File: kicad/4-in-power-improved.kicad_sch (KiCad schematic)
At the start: 45 parts, among them J1 USB_C_Receptacle_USB2.0_16P, J2 Bus_PCI_Express_x1, J3 Conn_01x02, U1 XC6206P332MR, U2 2P SMD 2.54P Jumper, U3 W25Q128JVP, U4 2P SMD 2.54P Jumper, U5 MCP25625T-E/ML, U6 RP2040, X1 ABM8-272-T3, Y1 X322516MLB4SI

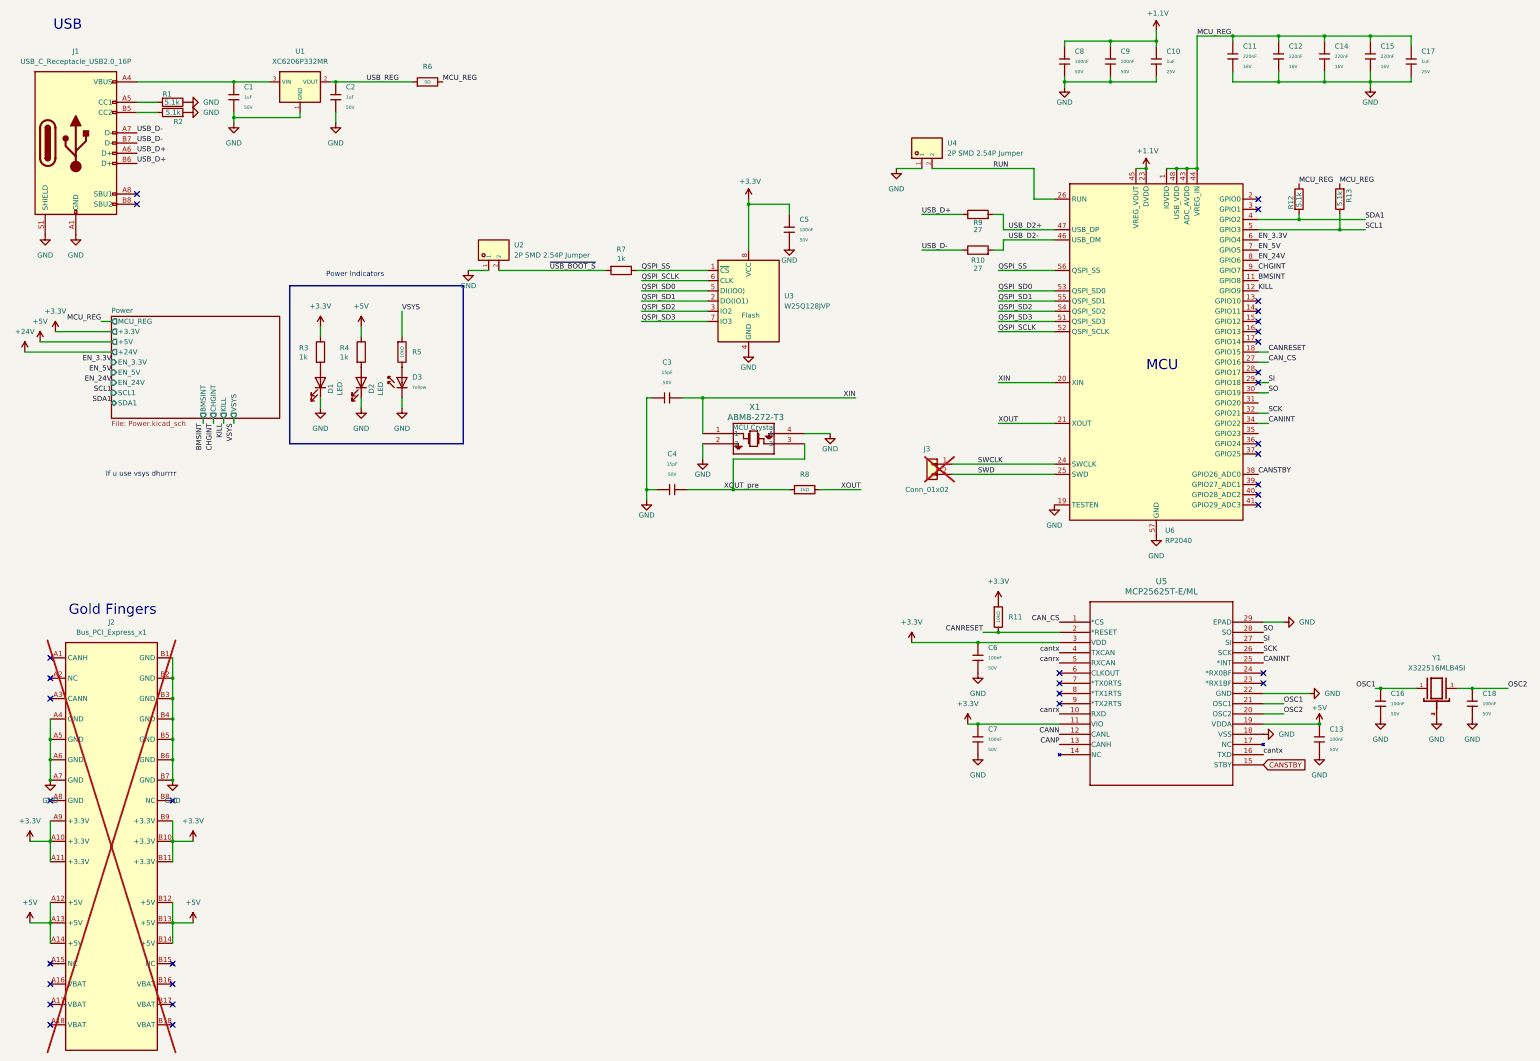
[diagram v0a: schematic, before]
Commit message: Charger IC footprint routed RP2040 routed BMS routed xt30s and balancers router
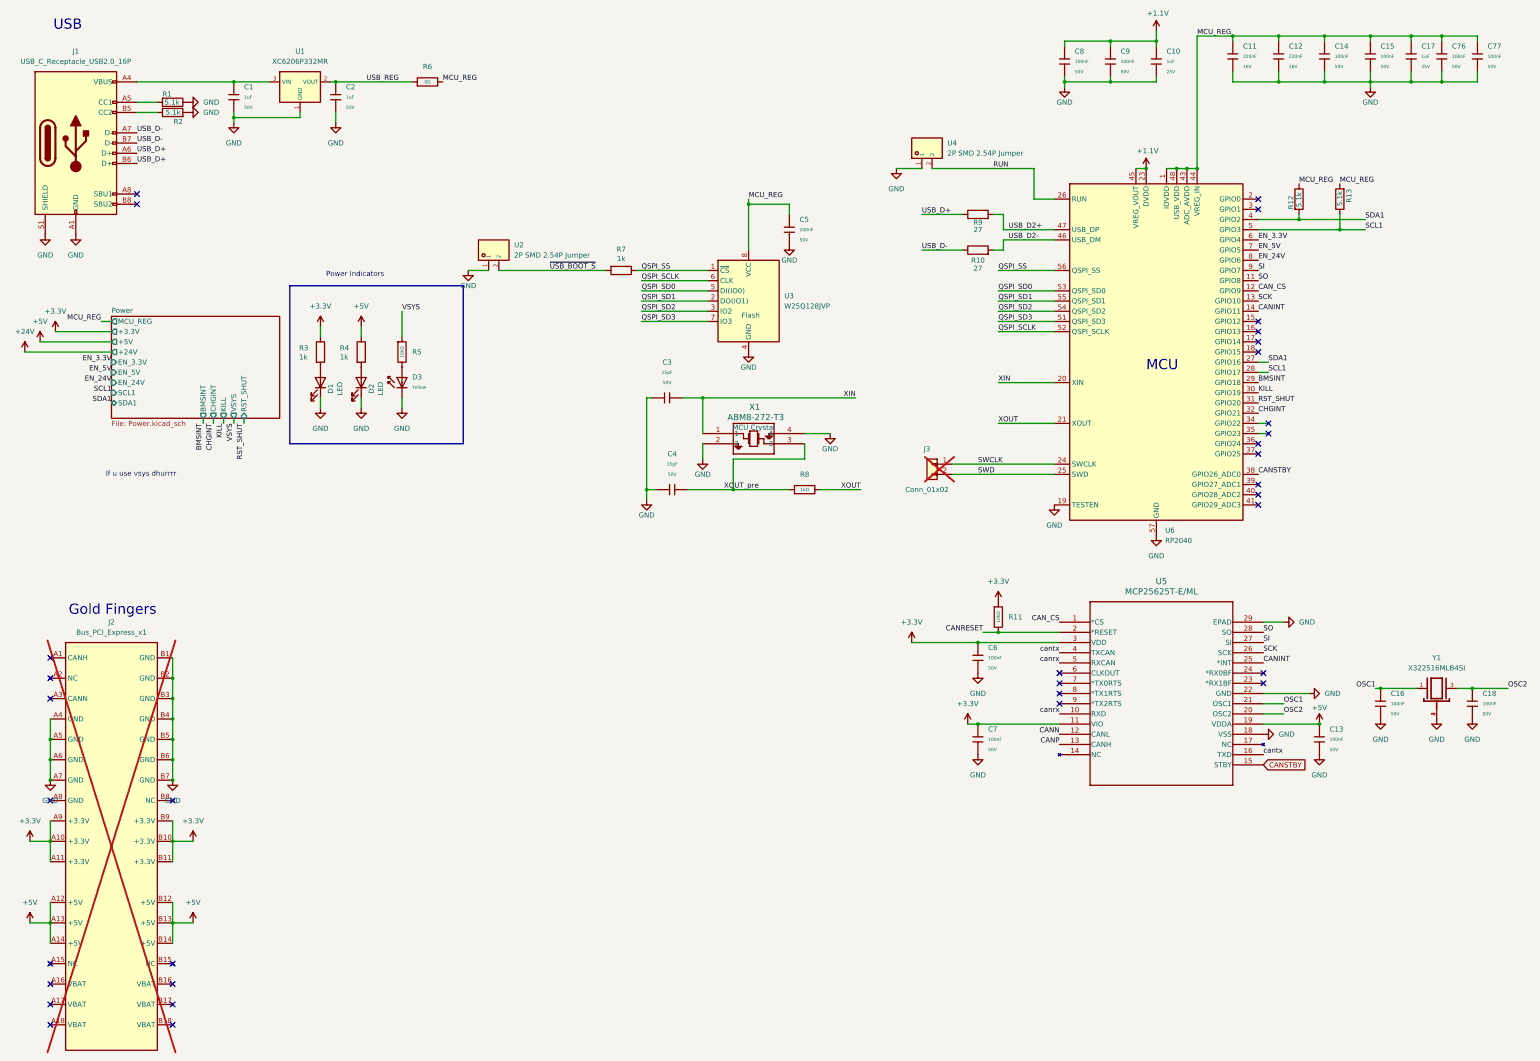
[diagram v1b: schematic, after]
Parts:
- removed C15: 220nF, PCM_JLCPCB:C_0402, symbol PCM_JLCPCB-Capacitors:0402,220nF
- removed R6: 0Ω, PCM_JLCPCB:R_0402, symbol PCM_JLCPCB-Resistors:0402,0Ω
- added C15, C76, C77: 100nF, PCM_JLCPCB:C_0402, symbol 4in-power:0402,100nF,(2)
- added R6: 0Ω, PCM_JLCPCB:R_0603, symbol PCM_JLCPCB-Resistors:0603,0Ω
- C14: value 220nF -> 100nF; symbol PCM_JLCPCB-Capacitors:0402,220nF -> 4in-power:0402,100nF,(2); Capacitance 220nF -> 100nF; LCSC C16772 -> C307331; Part CL05B224KO5NNNC -> CL05B104KB54PNC; Price 0.007USD -> 0.008USD; Stock 202070 -> 8389599; Voltage Rated 16V -> 50V
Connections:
- net +3.3V: no longer C5.1, U3.8 (VCC)
- net BMSINT: now also U6.29 (GPIO18); no longer U6.11 (GPIO8)
- net CANINT: now also U6.14 (GPIO11); no longer U6.34 (GPIO22)
- net CANRESET: no longer U6.18 (GPIO15)
- net CAN_CS: now also U6.12 (GPIO9); no longer U6.27 (GPIO16)
- net CHGINT: now also U6.32 (GPIO21); no longer U6.9 (GPIO7)
- net GND: now also C15.2, C76.2, C77.2
- net KILL: now also U6.30 (GPIO19); no longer U6.12 (GPIO9)
- net MCU_REG: now also C5.1, U3.8 (VCC), C15.1, C76.1, C77.1, R6.2
- net SCK: now also U6.13 (GPIO10); no longer U6.32 (GPIO21)
- net SCL1: now also U6.28 (GPIO17)
- net SDA1: now also U6.27 (GPIO16)
- net SI: now also U6.9 (GPIO7); no longer U6.29 (GPIO18)
- net SO: now also U6.11 (GPIO8); no longer U6.30 (GPIO19)
- net USB_REG: now also R6.1
- net RST_SHUT: now reaches U6.31 (GPIO20)
- no-connect marks 35 -> 34
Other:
- sheet Power ports: added RST_SHUT; removed none
- moved on the sheet: C17

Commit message: Footprint routing completed
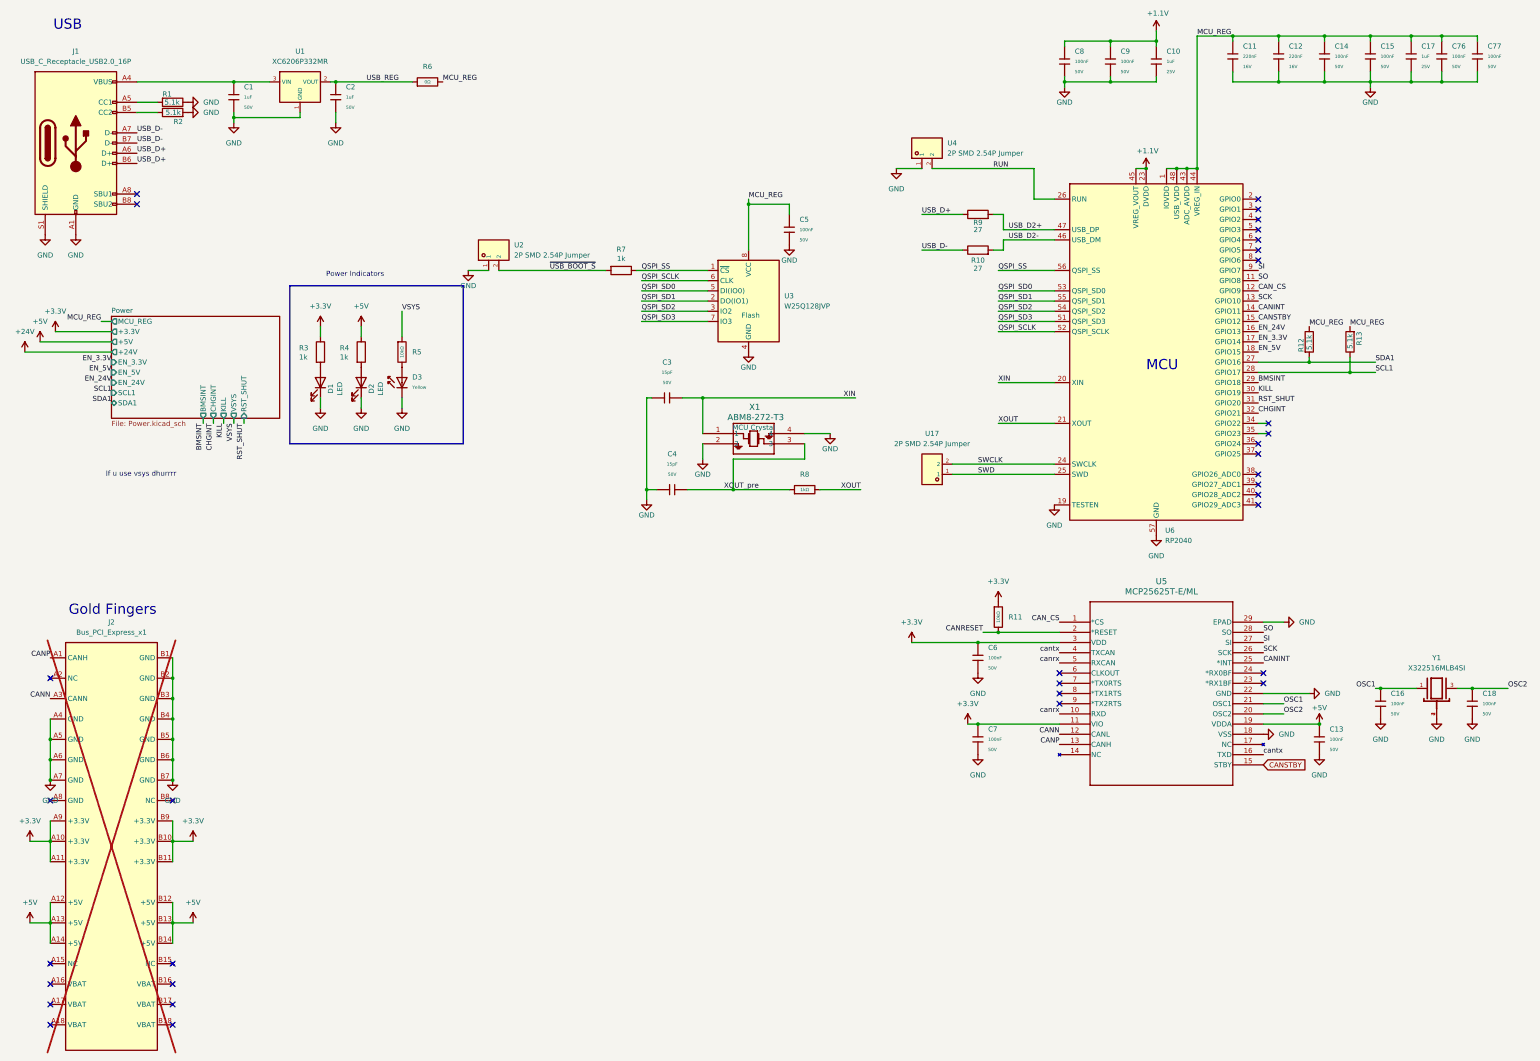
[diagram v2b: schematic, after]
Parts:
- removed J3: Conn_01x02, Connector_PinHeader_2.54mm:PinHeader_1x02_P2.54mm_Vertical, symbol Connector_Generic:Conn_01x02
- added U17: 2P SMD 2.54P Jumper, 4in-power:HDR-SMD_2P-P2.54-V-M-S4.8_DZ254S-11-02-50, symbol 4in-power:DZ254S-11-02-50
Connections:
- net CANN: now also J2.A3 (CANN)
- net CANP: now also J2.A1 (CANH)
- net CANSTBY: now also U6.15 (GPIO12); no longer U6.38 (GPIO26_ADC0)
- net EN_24V: now also U6.16 (GPIO13); no longer U6.8 (GPIO6)
- net EN_3.3V: now also U6.17 (GPIO14); no longer U6.6 (GPIO4)
- net EN_5V: now also U6.18 (GPIO15); no longer U6.7 (GPIO5)
- net SCL1: no longer U6.5 (GPIO3)
- net SDA1: no longer U6.4 (GPIO2)
- net SWCLK: now also U17.2
- net SWD: now also U17.1
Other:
- moved on the sheet: R12, R13

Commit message: Silk screen UI changes
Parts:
- added D17: Yellow, PCM_JLCPCB:D_0603, symbol PCM_JLCPCB-Diodes:LED,0603,Yellow
- added R57: 10kΩ, PCM_JLCPCB:R_0402, symbol 4in-power:0402,10kΩ
- added TP20, TP21, TP22, TP23, TP24: RH-5015, 4in-power:SMD_RH-5015, symbol 4in-power:RH-5015
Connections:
- net +24V: now also R57.1, TP20.1
- net +3.3V: now also TP22.1
- net +5V: now also TP21.1
- net GND: now also D17.1, TP23.1, TP24.1
- new net: D17.2, R57.2
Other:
- moved on the sheet: D1, D2, D3, R3, R4, R5

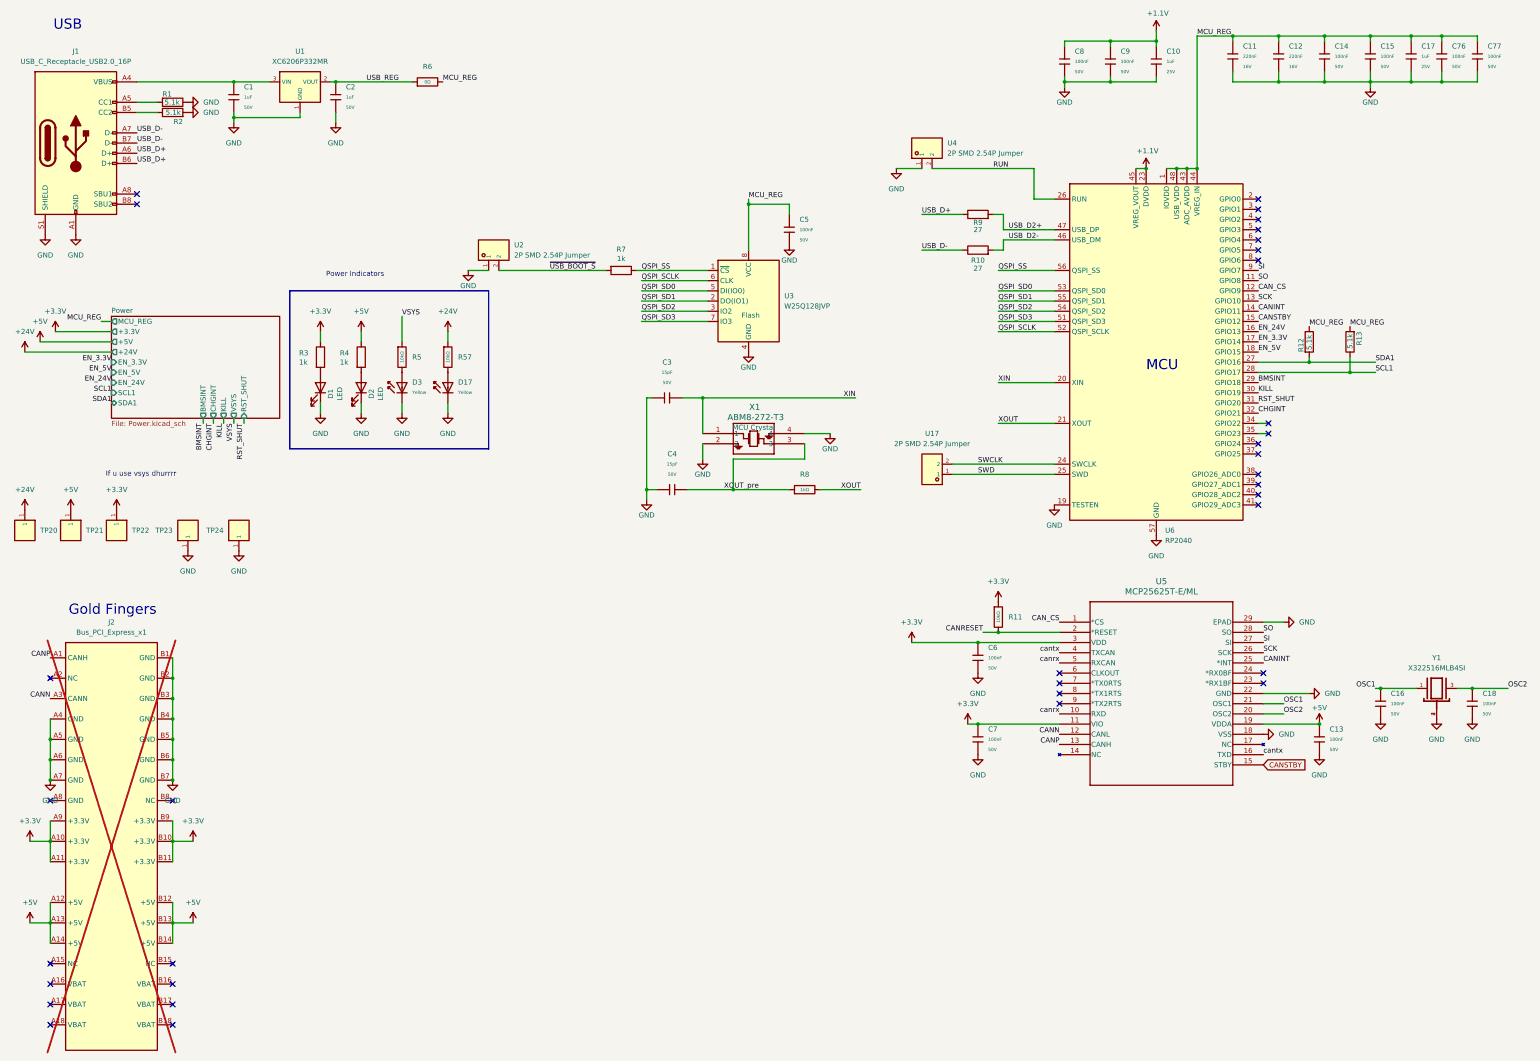
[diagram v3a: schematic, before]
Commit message: Fixed all silk screen solder mask issues, switched 24V Xt30 connector to JST 4P with CAN lines. Board is production ready
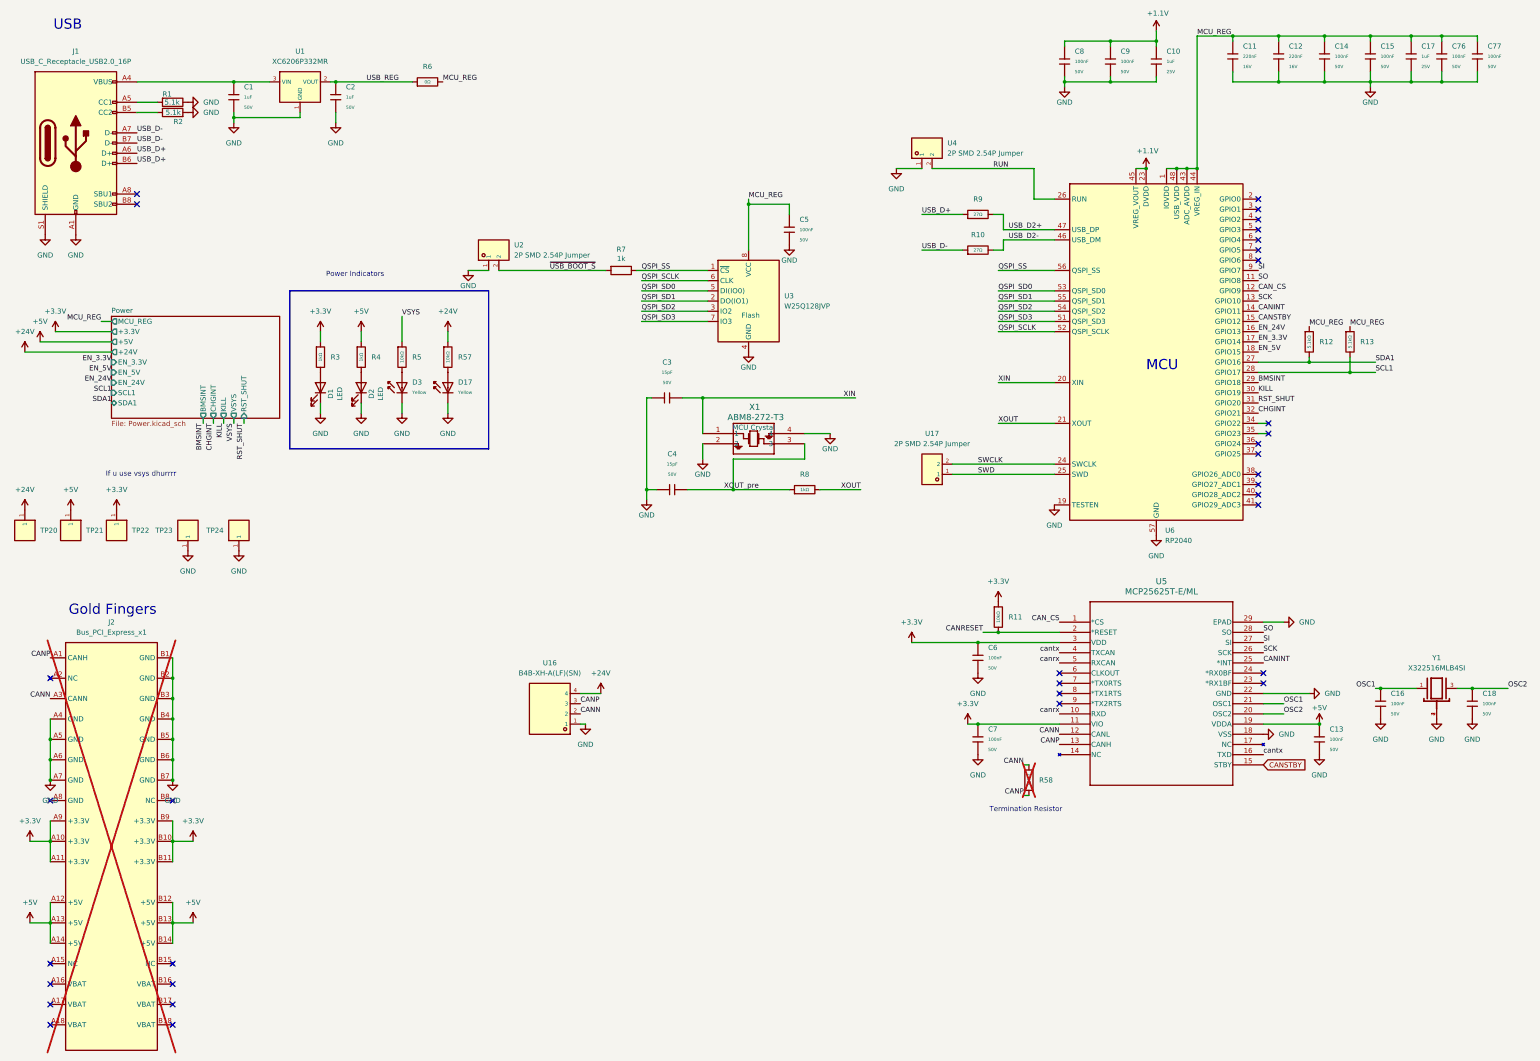
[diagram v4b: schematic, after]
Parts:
- removed R10, R9: 27, Resistor_SMD:R_0402_1005Metric, symbol Device:R
- removed R12, R13: 5.1k, Resistor_SMD:R_0402_1005Metric, symbol 4in-power:R
- removed R3, R4: 1k, Resistor_SMD:R_0402_1005Metric, symbol 4in-power:R
- added R10, R9: 27Ω, PCM_JLCPCB:R_0603, symbol PCM_JLCPCB-Resistors:0603,27Ω
- added R12, R13: 5.1kΩ, PCM_JLCPCB:R_0402, symbol PCM_JLCPCB-Resistors:0402,5.1kΩ
- added R3, R4: 1kΩ, PCM_JLCPCB:R_0402, symbol PCM_JLCPCB-Resistors:0402,1kΩ
- added R58: 120Ω, PCM_JLCPCB:R_1206, symbol PCM_JLCPCB-Resistors:1206,120Ω
- added U16: B4B-XH-A(LF)(SN), 4in-power:CONN-TH_B4B-XH-A-LF-SN, symbol 4in-power:B4B-XH-A(LF)(SN)
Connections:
- net +24V: now also U16.4
- net +3.3V: now also R3.1
- net +5V: now also R4.1
- net CANN: now also R58.1, U16.2
- net CANP: now also R58.2, U16.3
- net GND: now also U16.1
- net MCU_REG: now also R12.1, R13.1
- net SCL1: now also R13.2
- net SDA1: now also R12.2
- net USB_D+: now also R9.1
- net USB_D-: now also R10.1
- net USB_D2+: now also R9.2
- net USB_D2-: now also R10.2
- net at D1.2 (A): now also R3.2
- net at D2.2 (A): now also R4.2
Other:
- note added: "Termination Resistor"
